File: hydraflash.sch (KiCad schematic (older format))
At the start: 10 parts, among them J1 CONN_02X07, J2 CONN_02X10, J3 CONN_02X10, J4 CONN_01X06, P1 WRITE_PROTECT, U1 Flash_NAND

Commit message: Routing improvements by bvernoux
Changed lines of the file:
@@
 LIBS:contrib
 LIBS:valves
-LIBS:hydrabus-shield-template-cache
+LIBS:hydraflash-cache
 EELAYER 25 0
 EELAYER END
@@
 P 5250 3750
 F 0 "U1" H 5250 3750 60  0000 C CNN
-F 1 "Flash_NAND" H 5250 3750 60  0000 C CNN
+F 1 "Flash_NAND" H 5250 4500 60  0000 C CNN
 F 2 "tsop48_socket:TSOP48ZIF" H 5250 3750 60  0001 C CNN
 F 3 "" H 5250 3750 60  0000 C CNN

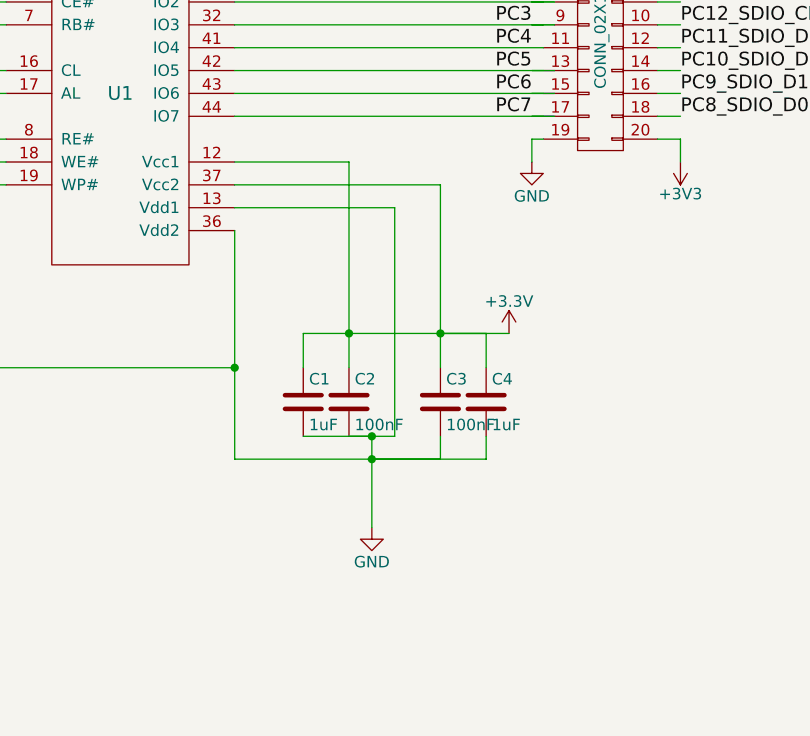
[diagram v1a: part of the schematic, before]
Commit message: Minor update(Capacitor values and 3V3 routing with bigger wire)
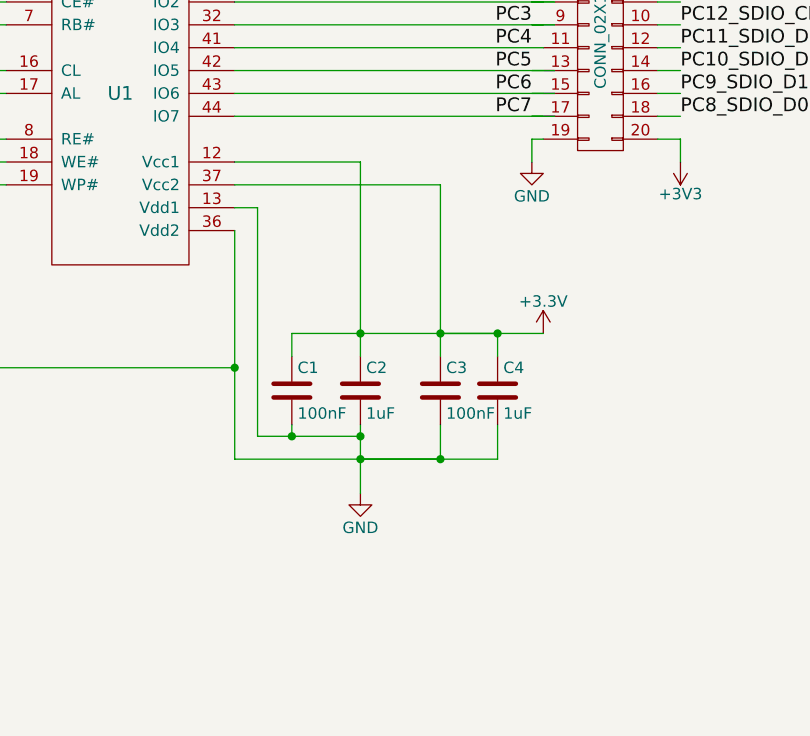
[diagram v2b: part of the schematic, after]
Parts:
- C1: value 1uF -> 100nF
- C2: value 100nF -> 1uF
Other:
- moved on the sheet: C1, C2, C3, C4
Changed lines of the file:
@@
 L C C2
 U 1 1 574F4079
-P 6250 5100
-F 0 "C2" H 6275 5200 50  0000 L CNN
-F 1 "100nF" H 6275 5000 50  0000 L CNN
-F 2 "Capacitors_SMD:C_0805_HandSoldering" H 6288 4950 50  0001 C CNN
-F 3 "" H 6250 5100 50  0000 C CNN
-	1    6250 5100
+P 6300 5050
+F 0 "C2" H 6325 5150 50  0000 L CNN
+F 1 "1uF" H 6325 4950 50  0000 L CNN
+F 2 "Capacitors_SMD:C_0805_HandSoldering" H 6338 4900 50  0001 C CNN
+F 3 "" H 6300 5050 50  0000 C CNN
+	1    6300 5050
 	1    0    0    -1
 $EndComp
@@
 	3150 3950 4750 3950
 Wire Wire Line
-	5750 4050 6250 4050
-Wire Wire Line
-	6250 4050 6250 4950
-Wire Wire Line
-	5750 4250 6450 4250
-Wire Wire Line
-	6450 4250 6450 5250
-Wire Wire Line
-	6450 5250 6250 5250
+	5750 4050 6300 4050
+Wire Wire Line
+	6300 4050 6300 4900
+Wire Wire Line
+	5750 4250 5850 4250
+Wire Wire Line
+	5850 4250 5850 5250
+Wire Wire Line
+	6300 5200 6300 5500
 $Comp
 L C C3
 U 1 1 574F4268
-P 6650 5100
-F 0 "C3" H 6675 5200 50  0000 L CNN
-F 1 "100nF" H 6675 5000 50  0000 L CNN
-F 2 "Capacitors_SMD:C_0805_HandSoldering" H 6688 4950 50  0001 C CNN
-F 3 "" H 6650 5100 50  0000 C CNN
-	1    6650 5100
+P 6650 5050
+F 0 "C3" H 6675 5150 50  0000 L CNN
+F 1 "100nF" H 6675 4950 50  0000 L CNN
+F 2 "Capacitors_SMD:C_0805_HandSoldering" H 6688 4900 50  0001 C CNN
+F 3 "" H 6650 5050 50  0000 C CNN
+	1    6650 5050
 	1    0    0    -1
 $EndComp
@@
 	5750 4150 6650 4150
 Wire Wire Line
-	6650 4150 6650 4950
+	6650 4150 6650 4900
 Wire Wire Line
 	5750 4350 5750 5350
 Wire Wire Line
-	5750 5350 6650 5350
-Wire Wire Line
-	6650 5350 6650 5250
+	5750 5350 6900 5350
+Wire Wire Line
+	6650 5350 6650 5200
 $Comp
 L +3.3V #PWR013
 U 1 1 574F44DB
-P 6950 4800
-F 0 "#PWR013" H 6950 4650 50  0001 C CNN
-F 1 "+3.3V" H 6950 4940 50  0000 C CNN
-F 2 "" H 6950 4800 50  0000 C CNN
-F 3 "" H 6950 4800 50  0000 C CNN
-	1    6950 4800
-	1    0    0    -1
-$EndComp
-Wire Wire Line
-	6050 4800 6950 4800
+P 7100 4800
+F 0 "#PWR013" H 7100 4650 50  0001 C CNN
+F 1 "+3.3V" H 7100 4940 50  0000 C CNN
+F 2 "" H 7100 4800 50  0000 C CNN
+F 3 "" H 7100 4800 50  0000 C CNN
+	1    7100 4800
+	1    0    0    -1
+$EndComp
+Wire Wire Line
+	6000 4800 7100 4800
 Connection ~ 6650 4800
-Connection ~ 6250 4800
+Connection ~ 6300 4800
 $Comp
 L GND #PWR014
 U 1 1 574F4612
-P 6350 5650
-F 0 "#PWR014" H 6350 5400 50  0001 C CNN
-F 1 "GND" H 6350 5500 50  0000 C CNN
-F 2 "" H 6350 5650 50  0000 C CNN
-F 3 "" H 6350 5650 50  0000 C CNN
-	1    6350 5650
-	1    0    0    -1
-$EndComp
-Wire Wire Line
-	6350 5250 6350 5650
-Connection ~ 6350 5350
-Connection ~ 6350 5250
+P 6300 5500
+F 0 "#PWR014" H 6300 5250 50  0001 C CNN
+F 1 "GND" H 6300 5350 50  0000 C CNN
+F 2 "" H 6300 5500 50  0000 C CNN
+F 3 "" H 6300 5500 50  0000 C CNN
+	1    6300 5500
+	1    0    0    -1
+$EndComp
+Connection ~ 6300 5350
+Connection ~ 6300 5250
 $Comp
 L CONN_01X02 P1
@@
 L C C1
 U 1 1 574F4E5E
-P 6050 5100
-F 0 "C1" H 6075 5200 50  0000 L CNN
-F 1 "1uF" H 6075 5000 50  0000 L CNN
-F 2 "Capacitors_SMD:C_0805_HandSoldering" H 6088 4950 50  0001 C CNN
-F 3 "" H 6050 5100 50  0000 C CNN
-	1    6050 5100
+P 6000 5050
+F 0 "C1" H 6025 5150 50  0000 L CNN
+F 1 "100nF" H 6025 4950 50  0000 L CNN
+F 2 "Capacitors_SMD:C_0805_HandSoldering" H 6038 4900 50  0001 C CNN
+F 3 "" H 6000 5050 50  0000 C CNN
+	1    6000 5050
 	1    0    0    -1
 $EndComp
@@
 L C C4
 U 1 1 574F4EA6
-P 6850 5100
-F 0 "C4" H 6875 5200 50  0000 L CNN
-F 1 "1uF" H 6875 5000 50  0000 L CNN
-F 2 "Capacitors_SMD:C_0805_HandSoldering" H 6888 4950 50  0001 C CNN
-F 3 "" H 6850 5100 50  0000 C CNN
-	1    6850 5100
-	1    0    0    -1
-$EndComp
-Wire Wire Line
-	6050 4950 6050 4800
-Wire Wire Line
-	6050 5250 6350 5250
-Wire Wire Line
-	6850 5250 6850 5350
-Wire Wire Line
-	6850 5350 6350 5350
-Wire Wire Line
-	6850 4950 6850 4800
-Wire Wire Line
-	6850 4800 6650 4800
+P 6900 5050
+F 0 "C4" H 6925 5150 50  0000 L CNN
+F 1 "1uF" H 6925 4950 50  0000 L CNN
+F 2 "Capacitors_SMD:C_0805_HandSoldering" H 6938 4900 50  0001 C CNN
+F 3 "" H 6900 5050 50  0000 C CNN
+	1    6900 5050
+	1    0    0    -1
+$EndComp
+Wire Wire Line
+	6000 4900 6000 4800
+Wire Wire Line
+	6900 5350 6900 5200
+Wire Wire Line
+	6650 5350 6300 5350
+Wire Wire Line
+	6900 4800 6900 4900
+Wire Wire Line
+	6650 4800 6900 4800
+Wire Wire Line
+	5850 5250 6300 5250
+Wire Wire Line
+	6000 5250 6000 5200
+Connection ~ 6900 4800
+Connection ~ 6650 5350
+Connection ~ 6000 5250
 $EndSCHEMATC
